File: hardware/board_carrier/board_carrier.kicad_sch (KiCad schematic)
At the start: 18 parts, among them J3 Conn_02x06_Top_Bottom, U1 TJA1051T-3, U2 LM78M05_TO252, U3 f042_wideband_module

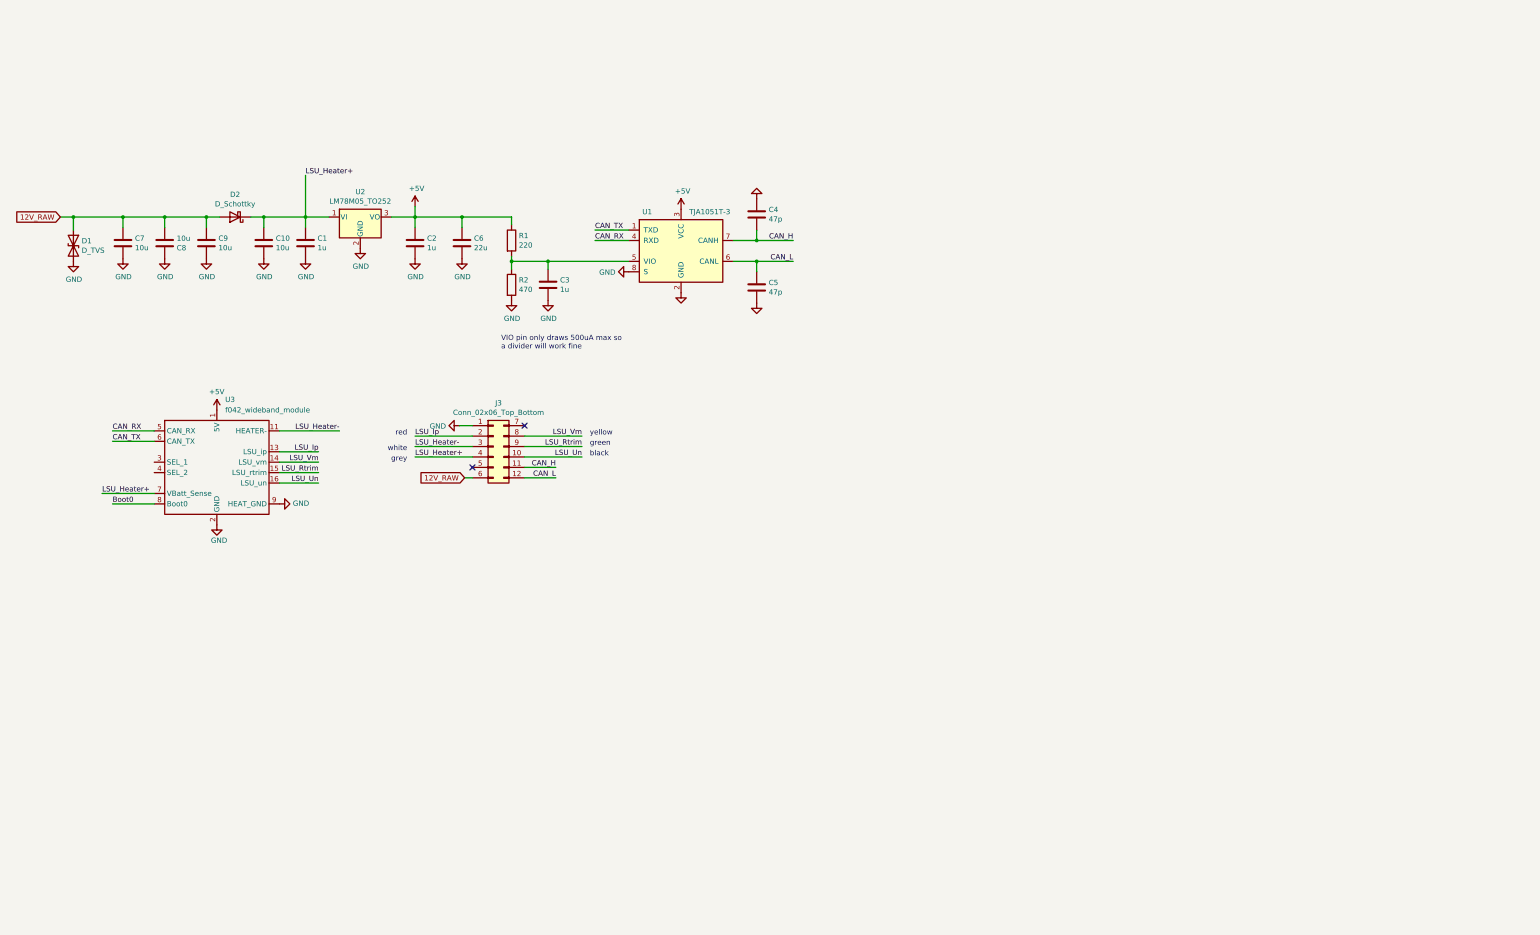
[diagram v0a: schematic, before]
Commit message: board_carrier: schematic generated from code (upstream carrier + analog output, TEST jumper, CAN terminator, op-amp supply clamp); ERC clean, netlist self-check in checks
Co-Authored-By: Claude Opus 5.5 <noreply@anthropic.com>
Claude-Session: https://claude.ai/code/session_01PSzkdckEqA8UiAsfxtaSyg
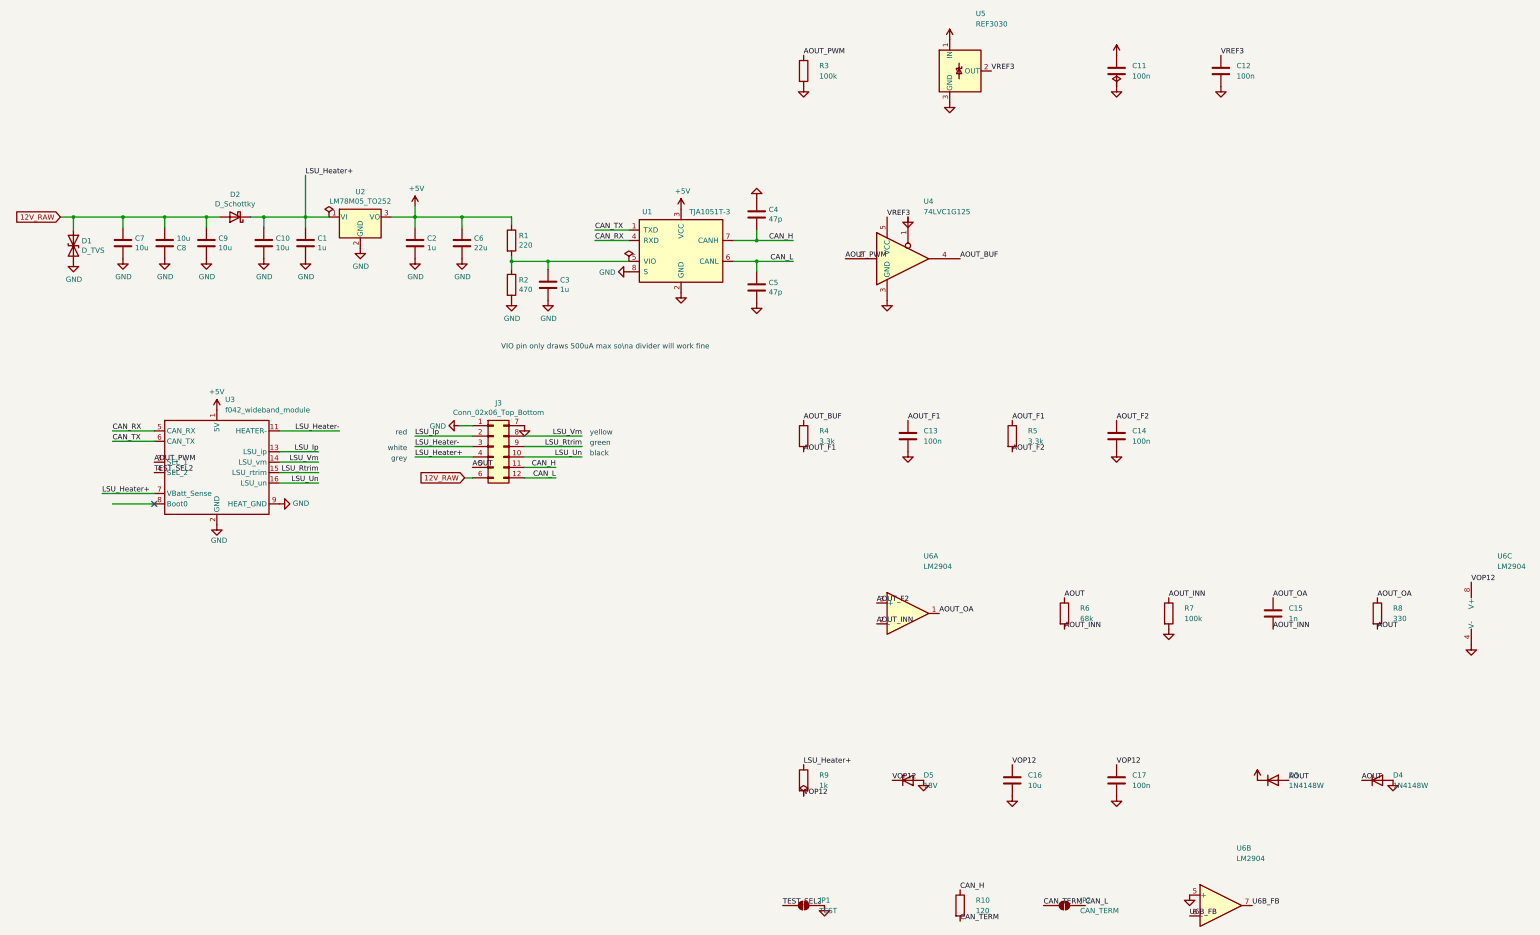
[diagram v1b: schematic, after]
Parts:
- added C11, C12, C13, C14, C17: 100n, Capacitor_SMD:C_0603_1608Metric, symbol Device:C
- added C15: 1n, Capacitor_SMD:C_0603_1608Metric, symbol Device:C
- added C16: 10u, Capacitor_SMD:C_1206_3216Metric, symbol Device:C
- added D3, D4: 1N4148W, Diode_SMD:D_SOD-123, symbol Diode:1N4148W
- added D5: 18V, Diode_SMD:D_SOD-123, symbol Device:D_Zener
- added JP1: TEST, Jumper:SolderJumper-2_P1.3mm_Open_RoundedPad1.0x1.5mm, symbol Jumper:SolderJumper_2_Open
- added JP2: CAN_TERM, Jumper:SolderJumper-2_P1.3mm_Open_RoundedPad1.0x1.5mm, symbol Jumper:SolderJumper_2_Open
- added R10: 120, Resistor_SMD:R_0603_1608Metric, symbol Device:R
- added R3, R7: 100k, Resistor_SMD:R_0603_1608Metric, symbol Device:R
- added R4, R5: 3.3k, Resistor_SMD:R_0603_1608Metric, symbol Device:R
- added R6: 68k, Resistor_SMD:R_0603_1608Metric, symbol Device:R
- added R8: 330, Resistor_SMD:R_0603_1608Metric, symbol Device:R
- added R9: 1k, Resistor_SMD:R_0603_1608Metric, symbol Device:R
- added U4: 74LVC1G125, Package_TO_SOT_SMD:SOT-353_SC-70-5, symbol 74xGxx:74LVC1G125
- added U5: REF3030, Package_TO_SOT_SMD:SOT-23, symbol Reference_Voltage:REF3030
- added U6: LM2904, Package_SO:SOIC-8_3.9x4.9mm_P1.27mm, symbol Amplifier_Operational:LM2904
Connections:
- net +5V: now also C11.1, D3.1 (K), U5.1 (IN)
- net CAN_H: now also R10.1
- net CAN_L: now also JP2.2 (B)
- net GND: now also J3.7 (Pin_7), C11.2, C12.2, C13.2, C14.2, C16.2, C17.2, D4.2 (A), D5.2 (A), JP1.2 (B), R3.2, R7.2, U4.1, U4.3 (GND), U5.3 (GND), U6.4 (V-), U6.5 (+)
- net LSU_Heater+: now also R9.1
- net AOUT: now reaches J3.5 (Pin_5)
- net AOUT: now also D3.2 (A), D4.1 (K), R6.1, R8.2
- net AOUT_PWM: now reaches U3.3 (SEL_1)
- net AOUT_PWM: now also R3.1, U4.2
- net TEST_SEL2: now reaches U3.4 (SEL_2)
- net TEST_SEL2: now also JP1.1 (A)
- net Boot0: no longer names the net of U3.8 (Boot0)
- new net AOUT_BUF: R4.1, U4.4
- new net AOUT_F1: C13.1, R4.2, R5.1
- new net AOUT_F2: C14.1, R5.2, U6.3 (+)
- new net AOUT_INN: C15.2, R6.2, R7.1, U6.2 (-)
- new net AOUT_OA: C15.1, R8.1, U6.1
- new net CAN_TERM: JP2.1 (A), R10.2
- new net U6B_FB: U6.6 (-), U6.7
- new net VOP12: C16.1, C17.1, D5.1 (K), R9.2, U6.8 (V+)
- new net VREF3: C12.1, U4.5 (VCC), U5.2 (OUT)
- no-connect marks 2 -> 1
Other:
- note added: "VIO pin only draws 500uA max so\na divider will work fine"
- note removed: "VIO pin only draws 500uA max so a divider will work fine"

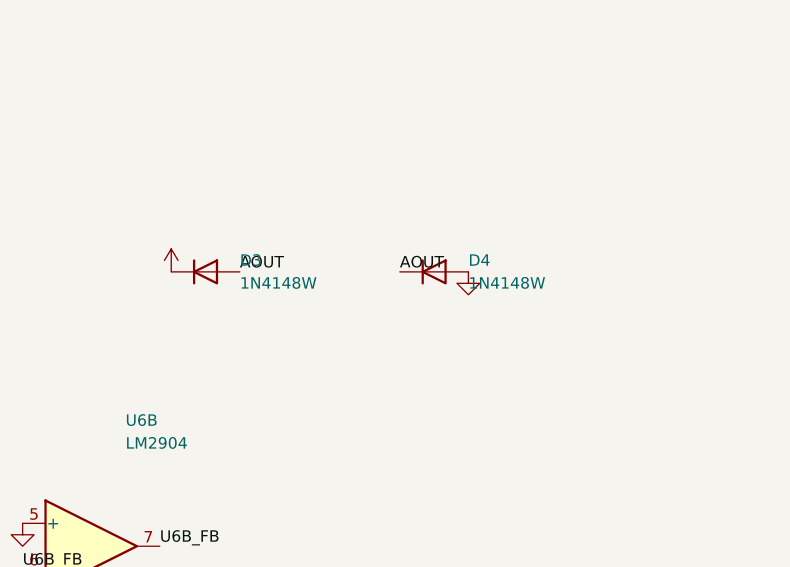
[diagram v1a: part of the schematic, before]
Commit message: board_carrier: annealing placer, GND fan-out and +5V tap vias, grid finisher after Freerouting, 0402 passives; 0 new DRC violations, 3 connections open (WIP)
work: checks/drc_vs_upstream.py (DRC minus upstream's baseline, in run_all), HANDOFF.md replaced with run history r6-r16 and the last raw output, STATE updated, R8/R9 power rating flagged for the audit

Co-Authored-By: Claude Opus 5.5 <noreply@anthropic.com>
Claude-Session: https://claude.ai/code/session_01PSzkdckEqA8UiAsfxtaSyg
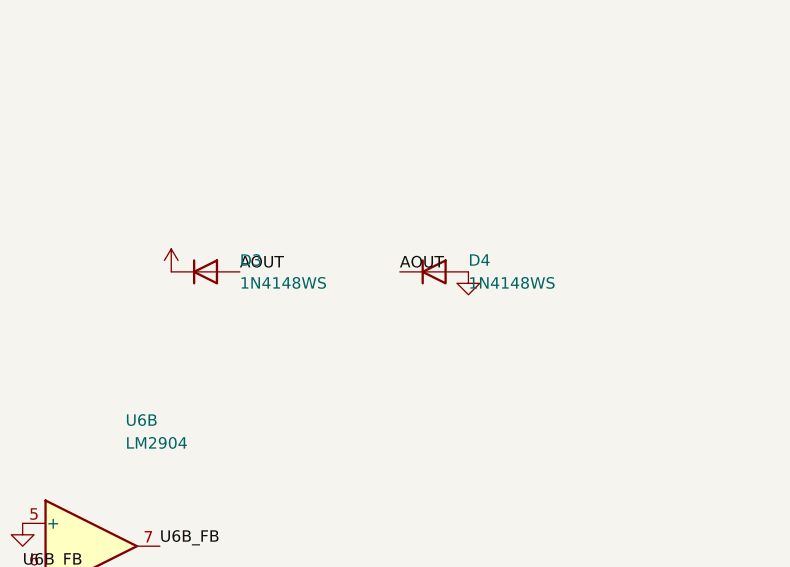
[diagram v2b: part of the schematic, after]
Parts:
- C11, C12, C13, C14: footprint Capacitor_SMD:C_0603_1608Metric -> Capacitor_SMD:C_0402_1005Metric; LCSC C14663 -> C1525
- C15: footprint Capacitor_SMD:C_0603_1608Metric -> Capacitor_SMD:C_0402_1005Metric; LCSC C1588 -> C1523
- D3, D4: value 1N4148W -> 1N4148WS; footprint Diode_SMD:D_SOD-123 -> Diode_SMD:D_SOD-323; symbol Diode:1N4148W -> Diode:1N4148WS; LCSC C81598 -> C2128
- R10: footprint Resistor_SMD:R_0603_1608Metric -> Resistor_SMD:R_0402_1005Metric; LCSC C22787 -> C25079
- R3, R7: footprint Resistor_SMD:R_0603_1608Metric -> Resistor_SMD:R_0402_1005Metric; LCSC C25803 -> C25741
- R4, R5: footprint Resistor_SMD:R_0603_1608Metric -> Resistor_SMD:R_0402_1005Metric; LCSC C22978 -> C25890
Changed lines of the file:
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@@
 			)
 		)
-		(property "Footprint" "Resistor_SMD:R_0603_1608Metric"
+		(property "Footprint" "Resistor_SMD:R_0402_1005Metric"
 			(at 215.9 40.64 0)
 			(hide yes)
@@
 			)
 		)
-		(property "LCSC" "C25803"
+		(property "LCSC" "C25741"
 			(at 215.9 40.64 0)
 			(hide yes)
@@
 			)
 		)
-		(property "Footprint" "Capacitor_SMD:C_0603_1608Metric"
+		(property "Footprint" "Capacitor_SMD:C_0402_1005Metric"
 			(at 292.1 40.64 0)
 			(hide yes)
@@
 			)
 		)
-		(property "LCSC" "C14663"
+		(property "LCSC" "C1525"
 			(at 292.1 40.64 0)
 			(hide yes)
@@
 			)
 		)
-		(property "Footprint" "Capacitor_SMD:C_0603_1608Metric"
+		(property "Footprint" "Capacitor_SMD:C_0402_1005Metric"
 			(at 317.5 40.64 0)
 			(hide yes)
@@
 			)
 		)
-		(property "LCSC" "C14663"
+		(property "LCSC" "C1525"
 			(at 317.5 40.64 0)
 			(hide yes)
@@
 			)
 		)
-		(property "Footprint" "Resistor_SMD:R_0603_1608Metric"
+		(property "Footprint" "Resistor_SMD:R_0402_1005Metric"
 			(at 215.9 129.54 0)
 			(hide yes)
@@
 			)
 		)
-		(property "LCSC" "C22978"
+		(property "LCSC" "C25890"
 			(at 215.9 129.54 0)
 			(hide yes)
@@
 			)
 		)
-		(property "Footprint" "Capacitor_SMD:C_0603_1608Metric"
+		(property "Footprint" "Capacitor_SMD:C_0402_1005Metric"
 			(at 241.3 129.54 0)
 			(hide yes)
@@
 			)
 		)
-		(property "LCSC" "C14663"
+		(property "LCSC" "C1525"
 			(at 241.3 129.54 0)
 			(hide yes)
@@
 			)
 		)
-		(property "Footprint" "Resistor_SMD:R_0603_1608Metric"
+		(property "Footprint" "Resistor_SMD:R_0402_1005Metric"
 			(at 266.7 129.54 0)
 			(hide yes)
@@
 			)
 		)
-		(property "LCSC" "C22978"
+		(property "LCSC" "C25890"
 			(at 266.7 129.54 0)
 			(hide yes)
@@
 			)
 		)
-		(property "Footprint" "Capacitor_SMD:C_0603_1608Metric"
+		(property "Footprint" "Capacitor_SMD:C_0402_1005Metric"
 			(at 292.1 129.54 0)
 			(hide yes)
@@
 			)
 		)
-		(property "LCSC" "C14663"
+		(property "LCSC" "C1525"
 			(at 292.1 129.54 0)
 			(hide yes)
@@
 			)
 		)
-		(property "Footprint" "Resistor_SMD:R_0603_1608Metric"
+		(property "Footprint" "Resistor_SMD:R_0402_1005Metric"
 			(at 304.8 172.72 0)
 			(hide yes)
@@
 			)
 		)
-		(property "LCSC" "C25803"
+		(property "LCSC" "C25741"
 			(at 304.8 172.72 0)
 			(hide yes)
@@
 			)
 		)
-		(property "Footprint" "Capacitor_SMD:C_0603_1608Metric"
+		(property "Footprint" "Capacitor_SMD:C_0402_1005Metric"
 			(at 330.2 172.72 0)
 			(hide yes)
@@
 			)
 		)
-		(property "LCSC" "C1588"
+		(property "LCSC" "C1523"
 			(at 330.2 172.72 0)
 			(hide yes)
@@
 	)
 	(symbol
-		(lib_id "Diode:1N4148W")
+		(lib_id "Diode:1N4148WS")
 		(at 330.2 213.36 0)
 		(unit 1)
@@
 			)
 		)
-		(property "Value" "1N4148W"
+		(property "Value" "1N4148WS"
 			(at 334.01 214.63 0)
 			(effects
@@
 			)
 		)
-		(property "Footprint" "Diode_SMD:D_SOD-123"
+		(property "Footprint" "Diode_SMD:D_SOD-323"
 			(at 330.2 213.36 0)
 			(hide yes)
@@
 			)
 		)
-		(property "LCSC" "C81598"
+		(property "LCSC" "C2128"
 			(at 330.2 213.36 0)
 			(hide yes)
@@
 	)
 	(symbol
-		(lib_id "Diode:1N4148W")
+		(lib_id "Diode:1N4148WS")
 		(at 355.6 213.36 0)
 		(unit 1)
@@
 			)
 		)
-		(property "Value" "1N4148W"
+		(property "Value" "1N4148WS"
 			(at 359.41 214.63 0)
 			(effects
@@
 			)
 		)
-		(property "Footprint" "Diode_SMD:D_SOD-123"
+		(property "Footprint" "Diode_SMD:D_SOD-323"
 			(at 355.6 213.36 0)
 			(hide yes)
@@
 			)
 		)
-		(property "LCSC" "C81598"
+		(property "LCSC" "C2128"
 			(at 355.6 213.36 0)
 			(hide yes)
@@
 			)
 		)
-		(property "Footprint" "Resistor_SMD:R_0603_1608Metric"
+		(property "Footprint" "Resistor_SMD:R_0402_1005Metric"
 			(at 254 243.84 0)
 			(hide yes)
@@
 			)
 		)
-		(property "LCSC" "C22787"
+		(property "LCSC" "C25079"
 			(at 254 243.84 0)
 			(hide yes)

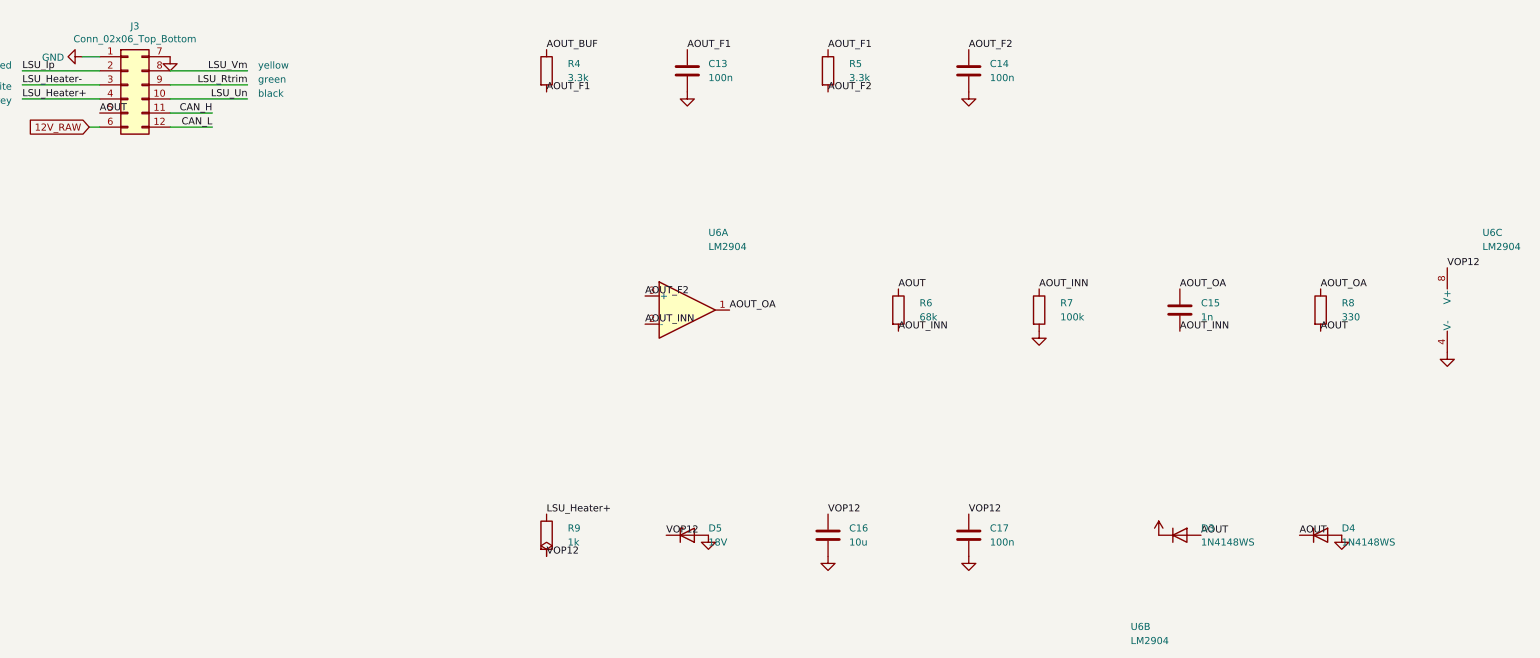
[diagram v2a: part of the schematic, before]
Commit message: board_carrier: board grown 15 mm (40.0 x 51.5 mm), analog stage in the new strip, R11 470R at J3-5 so a 12 V wiring fault can't back-feed +5V; 0 new DRC, 0 open, 0 vias in pads, 0 layout-review triggers (r36)
- gen_carrier_pcb: grow_board(), stage targets in the strip, upstream tracks all kept (REROUTE empty), bypass/Cf caps
  tied to their pins (C17 2.1 mm from U6 pin 8, was 4.5), CAN terminator moved off the output's corridor (r35)
- checks/layout_review.py (new, in checks.json): coupling, return paths, GND pour, as numbers
- sim/stability.sh topology D (R11): stable, 0.46 % low into 100k
- AGENTS.md rules 7-8: no assumed engineering decisions; layout changes re-checked by measurement
- docs/carrier.md: layout, review checklist, grounding analysis (J3-7 doc claim corrected), bring-up test A4
- RELEASE_ASSESSMENT/AUDIT/STATE/HANDOFF/LESSONS updated; new owner questions D7-D9

Co-Authored-By: Claude Opus 5.5 <noreply@anthropic.com>
Claude-Session: https://claude.ai/code/session_013ZVt2aLpmrSY8uzxABcZfb
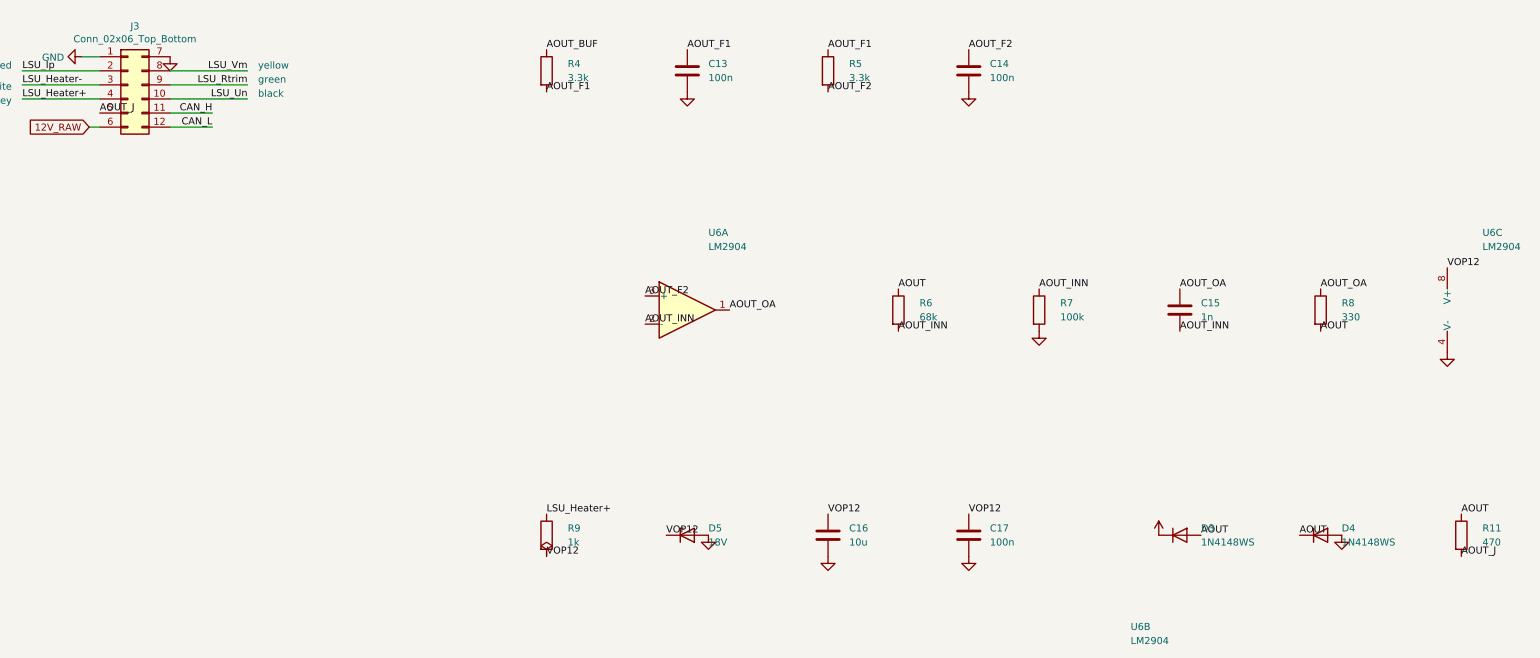
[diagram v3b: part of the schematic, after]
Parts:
- added R11: 470, Resistor_SMD:R_1206_3216Metric, symbol Device:R
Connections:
- net AOUT: now also R11.1; no longer J3.5 (Pin_5)
- new net AOUT_J: J3.5 (Pin_5), R11.2
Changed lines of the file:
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@@
+	(symbol
+		(lib_id "Device:R")
+		(at 381 213.36 0)
+		(unit 1)
+		(body_style 1)
+		(exclude_from_sim no)
+		(in_bom yes)
+		(on_board yes)
+		(in_pos_files yes)
+		(dnp no)
+		(property "Reference" "R11"
+			(at 384.81 212.09 0)
+			(effects
+				(font
+					(size 1.27 1.27)
+				)
+				(justify left)
+			)
+		)
+		(property "Value" "470"
+			(at 384.81 214.63 0)
+			(effects
+				(font
+					(size 1.27 1.27)
+				)
+				(justify left)
+			)
+		)
+		(property "Footprint" "Resistor_SMD:R_1206_3216Metric"
+			(at 381 213.36 0)
+			(hide yes)
+			(effects
+				(font
+					(size 1.27 1.27)
+				)
+				(justify left)
+			)
+		)
+		(property "Datasheet" ""
+			(at 381 213.36 0)
+			(hide yes)
+			(effects
+				(font
+					(size 1.27 1.27)
+				)
+				(justify left)
+			)
+		)
+		(property "Description" ""
+			(at 381 213.36 0)
+			(hide yes)
+			(effects
+				(font
+					(size 1.27 1.27)
+				)
+				(justify left)
+			)
+		)
+		(property "LCSC" "C4502"
+			(at 381 213.36 0)
+			(hide yes)
+			(effects
+				(font
+					(size 1.27 1.27)
+				)
+				(justify left)
+			)
+		)
+		(pin "1"
+		)
+		(pin "2"
+		)
+	)
 	(symbol
 		(lib_id "Device:R")
@@
 	)
 	(label "AOUT"
+		(at 381 209.55 0)
+		(effects
+			(font
+				(size 1.27 1.27)
+			)
+			(justify left bottom)
+		)
+	)
+	(label "AOUT_J"
+		(at 381 217.17 0)
+		(effects
+			(font
+				(size 1.27 1.27)
+			)
+			(justify left bottom)
+		)
+	)
+	(label "AOUT_J"
 		(at 135.255 137.16 0)
 		(effects
